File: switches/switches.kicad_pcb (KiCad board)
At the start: 2 copper layers, 50 x 90 mm, 45 parts, among them J1 switchesOut, J10 Conn_01x01_Female, J11 Conn_01x01_Female, J12 Conn_01x01_Female, J2 Conn_01x01_Female, J3 Conn_01x01_Female, J4 Conn_01x01_Female, J5 Conn_01x01_Female, J6 Conn_01x01_Female, J7 Conn_01x01_Female, J8 Conn_01x01_Female, J9 Conn_01x01_Female, Q1 2N7002, Q2 2N7002, Q3 2N7002, Q4 2N7002, Q5 2N7002, Q6 2N7002

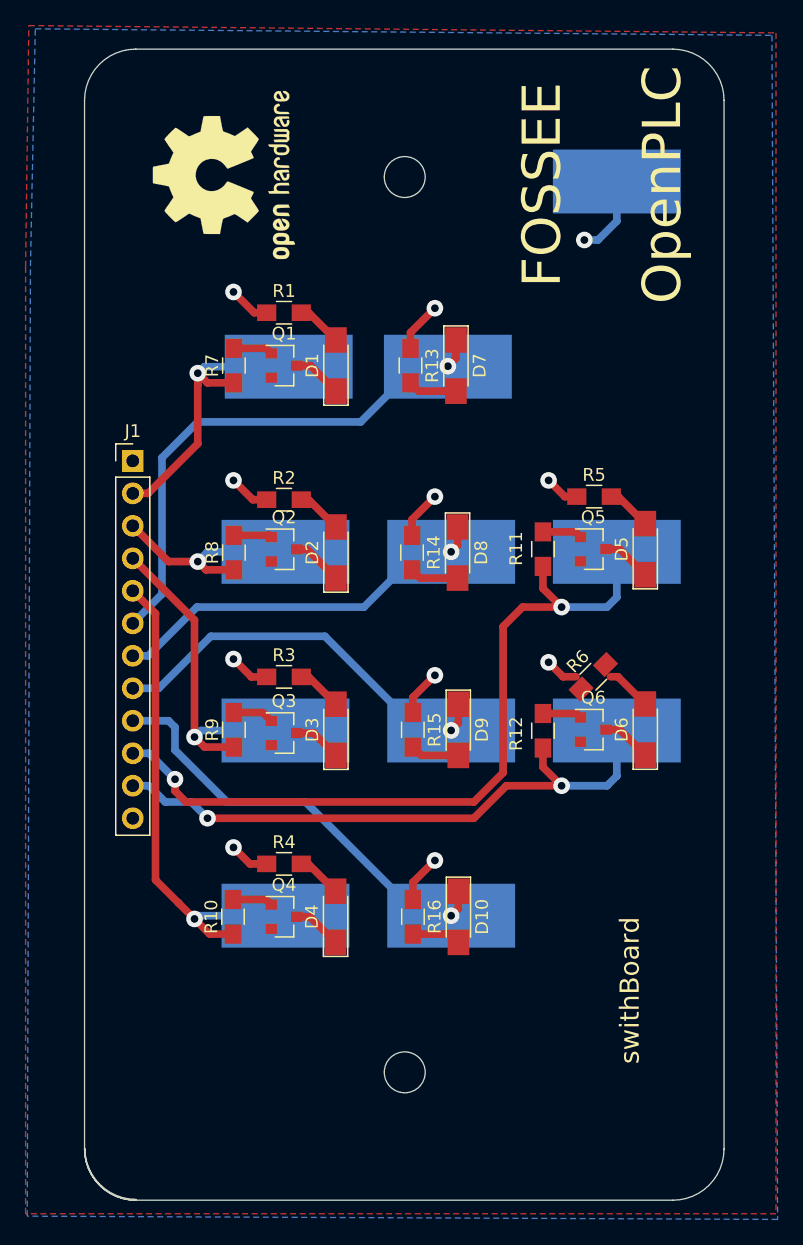
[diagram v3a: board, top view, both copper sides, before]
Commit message: created .csv bom file & also created interactive-html-bom for eac module
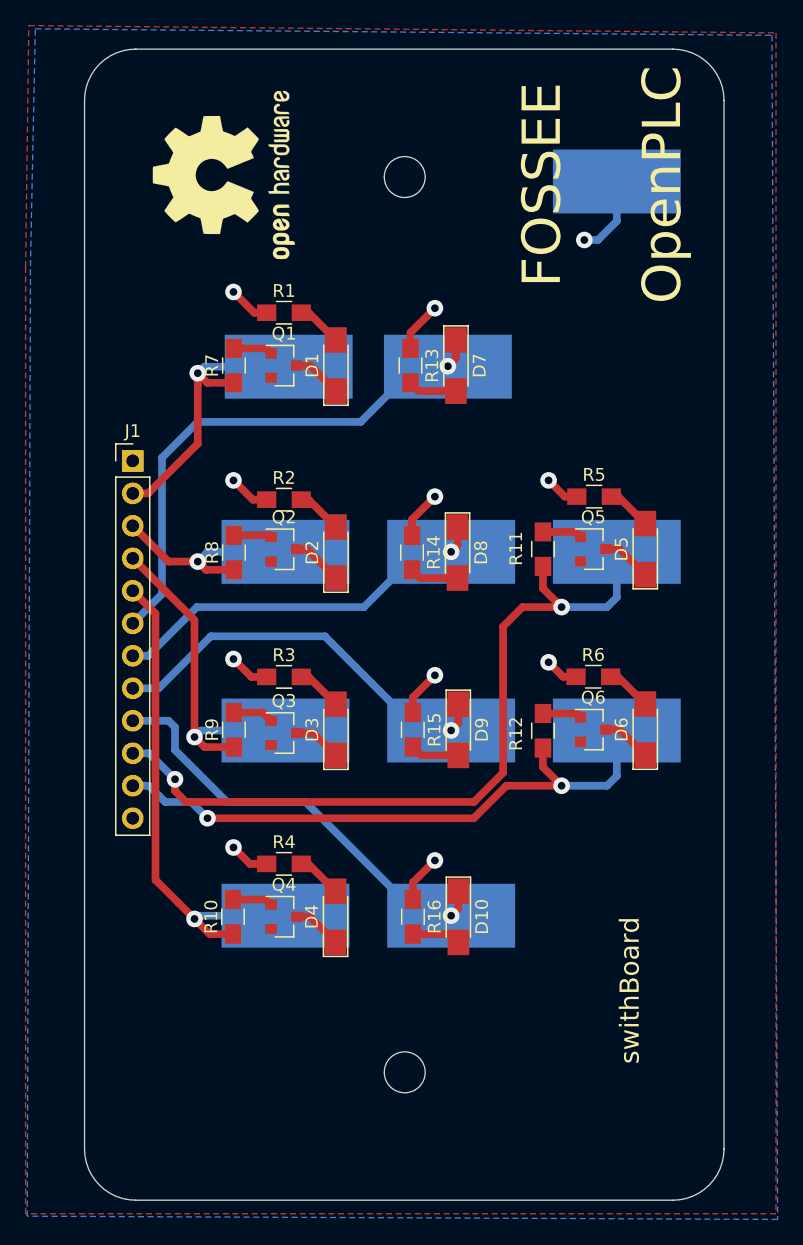
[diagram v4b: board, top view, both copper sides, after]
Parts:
- turned R6 to 0 degrees
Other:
- outline, holes or cut-outs redrawn
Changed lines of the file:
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@@
   (general
     (thickness 1.6)
-    (drawings 17)
+    (drawings 15)
     (tracks 175)
     (zones 0)
@@
   )
   (module Resistors_SMD:R_0805_HandSoldering (layer F.Cu)
-    (at 133.8 100.44345 45)
+    (at 133.8 100.44345)
     (descr "Resistor SMD 0805, hand soldering")
     (tags "resistor 0805")
     (attr smd)
-    (fp_text reference R6 (at 0 -1.7 45) (layer F.SilkS)
-      (effects (font (size 1 1) (thickness 0.15)))
-    )
-    (fp_text value R_US (at 0 1.75 45) (layer F.Fab)
-      (effects (font (size 1 1) (thickness 0.15)))
-    )
-    (fp_text user %R (at 0 0 45) (layer F.Fab)
+    (fp_text reference R6 (at 0 -1.7) (layer F.SilkS)
+      (effects (font (size 1 1) (thickness 0.15)))
+    )
+    (fp_text value R_US (at 0 1.75) (layer F.Fab)
+      (effects (font (size 1 1) (thickness 0.15)))
+    )
+    (fp_text user %R (at 0 0) (layer F.Fab)
       (effects (font (size 0.5 0.5) (thickness 0.075)))
     )
@@
     (fp_line (start 2.35 0.9) (end 2.35 -0.9) (layer F.CrtYd) (width 0.05))
     (fp_line (start 2.35 0.9) (end -2.35 0.9) (layer F.CrtYd) (width 0.05))
-    (pad 1 smd rect (at -1.35 0 45) (size 1.5 1.3) (layers F.Cu F.Paste F.Mask)
+    (pad 1 smd rect (at -1.35 0) (size 1.5 1.3) (layers F.Cu F.Paste F.Mask)
       (net 19 +5V))
-    (pad 2 smd rect (at 1.35 0 45) (size 1.5 1.3) (layers F.Cu F.Paste F.Mask)
+    (pad 2 smd rect (at 1.35 0) (size 1.5 1.3) (layers F.Cu F.Paste F.Mask)
       (net 24 "Net-(D6-Pad2)"))
     (model ${KISYS3DMOD}/Resistors_SMD.3dshapes/R_0805.wrl
@@
       (effects (font (size 1 1) (thickness 0.15)))
     )
-    (fp_text value switchesOut (at 0 30.27) (layer F.Fab)
+    (fp_text value switchesOut (at 1.21 30.734) (layer F.Fab)
       (effects (font (size 1 1) (thickness 0.15)))
     )
@@
       (xy -0.026262 -5.547126) (xy 0 -5.547126) (xy 0.209014 -5.547002)) (layer F.SilkS) (width 0.01))
   )
+  (gr_line (start 140.018 141.372) (end 98.018 141.372) (layer Edge.Cuts) (width 0.1))
+  (gr_line (start 140.018 51.372) (end 98.018 51.372) (layer Edge.Cuts) (width 0.1))
+  (gr_line (start 94.018 55.372) (end 94.018 137.372) (layer Edge.Cuts) (width 0.1))
+  (gr_arc (start 140.018 137.372) (end 140.018 141.372) (angle -90) (layer Edge.Cuts) (width 0.1))
+  (gr_line (start 144.018 137.372) (end 144.018 55.372) (layer Edge.Cuts) (width 0.1))
+  (gr_arc (start 140.018 55.372) (end 144.018 55.372) (angle -90) (layer Edge.Cuts) (width 0.1))
+  (gr_arc (start 98.018 55.372) (end 98.018 51.372) (angle -90) (layer Edge.Cuts) (width 0.1))
+  (gr_circle (center 119.053327 61.372) (end 119.053327 59.771999) (layer Edge.Cuts) (width 0.1))
   (dimension 50.0001 (width 0.3) (layer Margin)
     (gr_text "50.000 mm" (at 118.973596 42.647849 0.1145914062) (layer Margin)
@@
   )
   (gr_circle (center 119.053327 131.372) (end 119.053327 129.772) (layer Edge.Cuts) (width 0.1))
-  (gr_arc (start 98.044 137.308) (end 94.044 137.308) (angle -90) (layer Edge.Cuts) (width 0.1))
   (gr_arc (start 98.018 137.372) (end 94.018 137.372) (angle -90) (layer Edge.Cuts) (width 0.1))
-  (gr_line (start 140.018 141.372) (end 98.018 141.372) (layer Edge.Cuts) (width 0.1))
-  (gr_line (start 140.018 51.372) (end 98.018 51.372) (layer Edge.Cuts) (width 0.1))
-  (gr_arc (start 140.018 55.372) (end 144.018 55.372) (angle -90) (layer Edge.Cuts) (width 0.1))
-  (gr_line (start 144.018 137.372) (end 144.018 55.372) (layer Edge.Cuts) (width 0.1))
-  (gr_arc (start 140.018 137.372) (end 140.018 141.372) (angle -90) (layer Edge.Cuts) (width 0.1))
-  (gr_arc (start 98.018 137.372) (end 94.018 137.372) (angle -90) (layer Edge.Cuts) (width 0.1))
-  (gr_line (start 94.018 55.372) (end 94.018 137.372) (layer Edge.Cuts) (width 0.1))
-  (gr_arc (start 98.018 55.372) (end 98.018 51.372) (angle -90) (layer Edge.Cuts) (width 0.1))
-  (gr_circle (center 119.053327 61.372) (end 119.053327 59.771999) (layer Edge.Cuts) (width 0.1))
   (gr_text swithBoard (at 136.652 124.968 90) (layer F.SilkS)
     (effects (font (size 1.5 1.5) (thickness 0.3)))

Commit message: gerbers generate
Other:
- board text added: "switchBoard"
- board text removed: "swithBoard"
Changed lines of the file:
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@@
       (outputformat 1)
       (mirror false)
-      (drillshape 1)
+      (drillshape 0)
       (scaleselection 1)
-      (outputdirectory ""))
+      (outputdirectory "gerber/"))
   )
   (net 0 "")
@@
   (gr_circle (center 119.053327 131.372) (end 119.053327 129.772) (layer Edge.Cuts) (width 0.1))
   (gr_arc (start 98.018 137.372) (end 94.018 137.372) (angle -90) (layer Edge.Cuts) (width 0.1))
-  (gr_text swithBoard (at 136.652 124.968 90) (layer F.SilkS)
+  (gr_text switchBoard (at 136.652 124.968 90) (layer F.SilkS)
     (effects (font (size 1.5 1.5) (thickness 0.3)))
   )
